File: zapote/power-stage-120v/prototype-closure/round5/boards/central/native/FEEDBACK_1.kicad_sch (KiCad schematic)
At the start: 6 parts

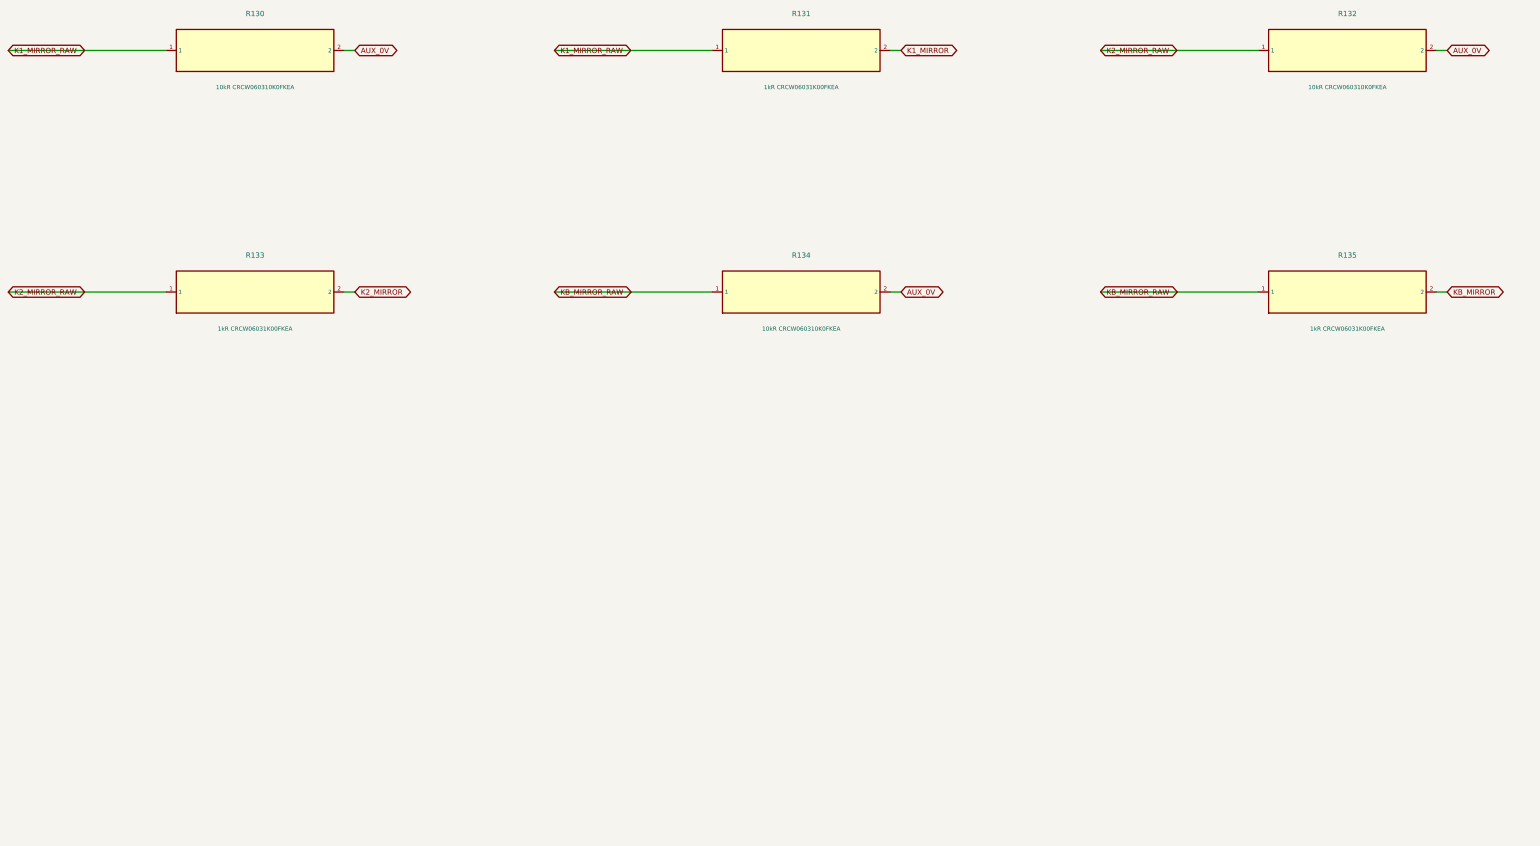
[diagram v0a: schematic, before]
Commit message: WIP snapshot of worktrees/mit-product-guidance (2026-10-08)
Uncommitted Codex prototype-closure work (round5 boards, round6
investigation, firmware power adapter), snapshotted without touching the
worktree. Raw solver output under output/temper-prototype-closure/ is
not included.

Co-Authored-By: Claude Opus 5.5 (1M context) <noreply@anthropic.com>
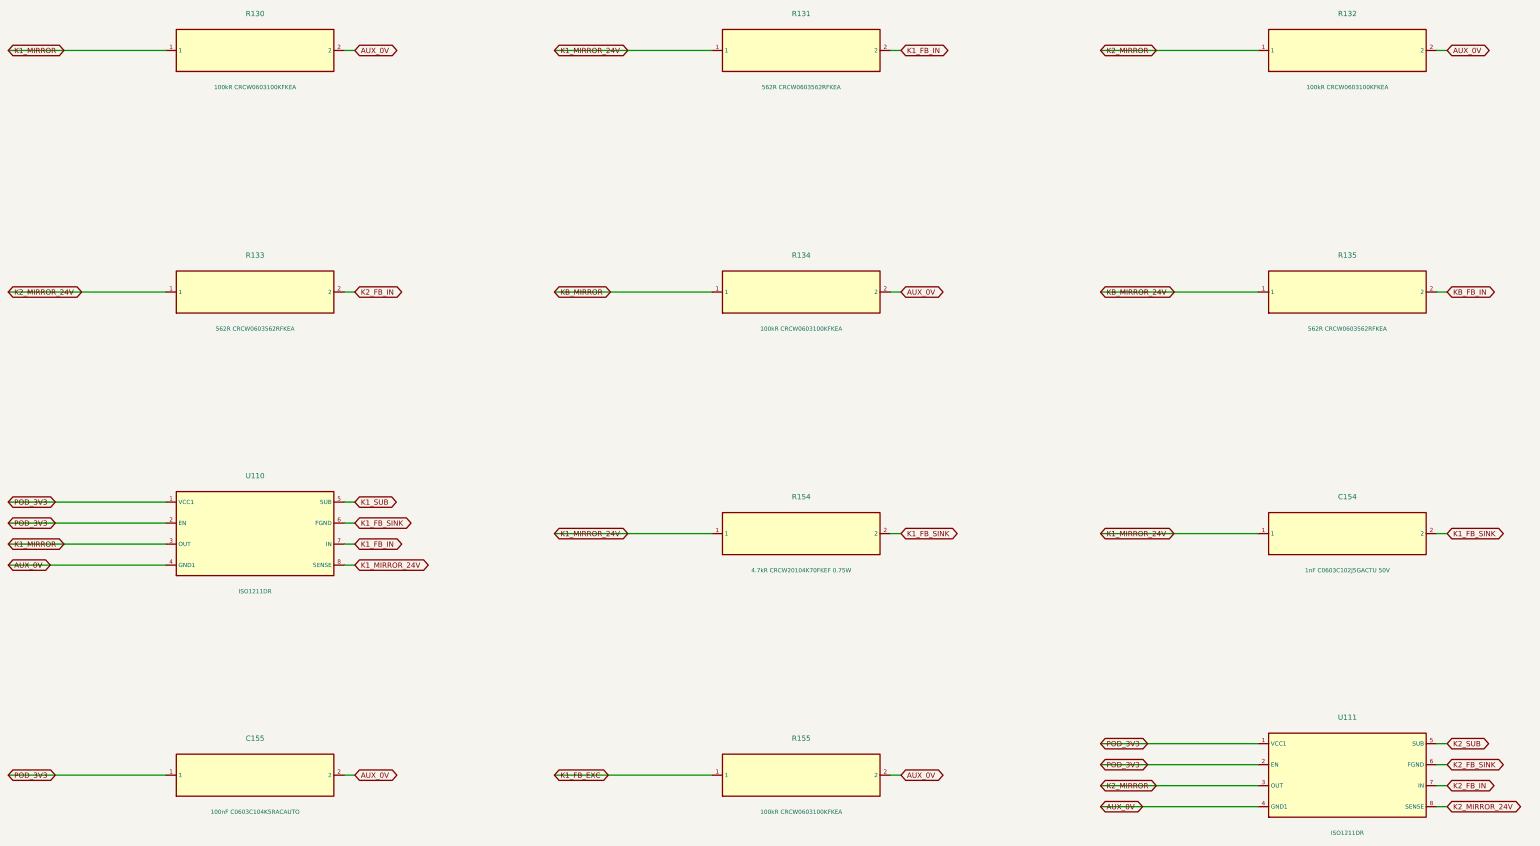
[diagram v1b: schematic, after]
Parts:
- added C154: 1nF C0603C102J5GACTU 50V, Capacitor_SMD:C_0603_1608Metric, symbol Supervisor:Part_C154
- added C155: 100nF C0603C104K5RACAUTO, Capacitor_SMD:C_0603_1608Metric, symbol Supervisor:Part_C155
- added R154: 4.7kR CRCW20104K70FKEF 0.75W, Resistor_SMD:R_2010_5025Metric, symbol Supervisor:Part_R154
- added R155: 100kR CRCW0603100KFKEA, Resistor_SMD:R_0603_1608Metric, symbol Supervisor:Part_R155
- added U110: ISO1211DR, Package_SO:SOIC-8_3.9x4.9mm_P1.27mm, symbol Supervisor:Part_U110
- added U111: ISO1211DR, Package_SO:SOIC-8_3.9x4.9mm_P1.27mm, symbol Supervisor:Part_U111
- R130, R132, R134: value 10kR CRCW060310K0FKEA -> 100kR CRCW0603100KFKEA
- R131, R133, R135: value 1kR CRCW06031K00FKEA -> 562R CRCW0603562RFKEA
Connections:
- net AUX_0V: now also C155.2, R155.2, U110.4 (GND1), U111.4 (GND1)
- net K1_MIRROR: now also R130.1, U110.3 (OUT); no longer R131.2
- net K2_MIRROR: now also R132.1, U111.3 (OUT); no longer R133.2
- net KB_MIRROR: now also R134.1; no longer R135.2
- net K1_MIRROR_RAW renamed K1_MIRROR_24V
- net K1_MIRROR_24V: now also C154.1, R154.1, U110.8 (SENSE); no longer R130.1
- net K2_MIRROR_RAW renamed K2_MIRROR_24V
- net K2_MIRROR_24V: now also U111.8 (SENSE); no longer R132.1
- net KB_MIRROR_RAW renamed KB_MIRROR_24V
- net KB_MIRROR_24V: no longer R134.1
- new net K1_FB_EXC: R155.1
- new net K1_FB_IN: R131.2, U110.7 (IN)
- new net K1_FB_SINK: C154.2, R154.2, U110.6 (FGND)
- new net K1_SUB: U110.5 (SUB)
- new net K2_FB_IN: R133.2, U111.7 (IN)
- new net K2_FB_SINK: U111.6 (FGND)
- new net K2_SUB: U111.5 (SUB)
- new net KB_FB_IN: R135.2
- new net POD_3V3: C155.1, U110.1 (VCC1), U110.2 (EN), U111.1 (VCC1), U111.2 (EN)
